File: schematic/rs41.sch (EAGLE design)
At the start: 267 parts, among them J201 SENSORBOOM, J601 expansion, J602 XDATA, Q201 BSS92, Q202 BSS92, Q203 BSS101, Q204 BSS101, Q501 BSS92, Q502 BSS101, Q503 BSS101, Q601 BSS101, U101 STM32F100C8T6B, U201 TS3A4751, U202 TS5A9411, U203 TS5A9411, U204 TS5A9411, U205 74HCU04, U206 305G, U207 74LVC3G34, U208 Z27F, U301 DIFFGEN, U302 UBX-6010MLF56, U303 SAW, U304 LNA, U401 SI4032QFN204X4, U501 TLV70030SOT23-5, U502 TPS61200, U503 TLV70030SOT23-5, U504 TLV70030SOT23-5, U601 25AA080SN, X101 24MHz, X301 OSC_GPSXTAL4

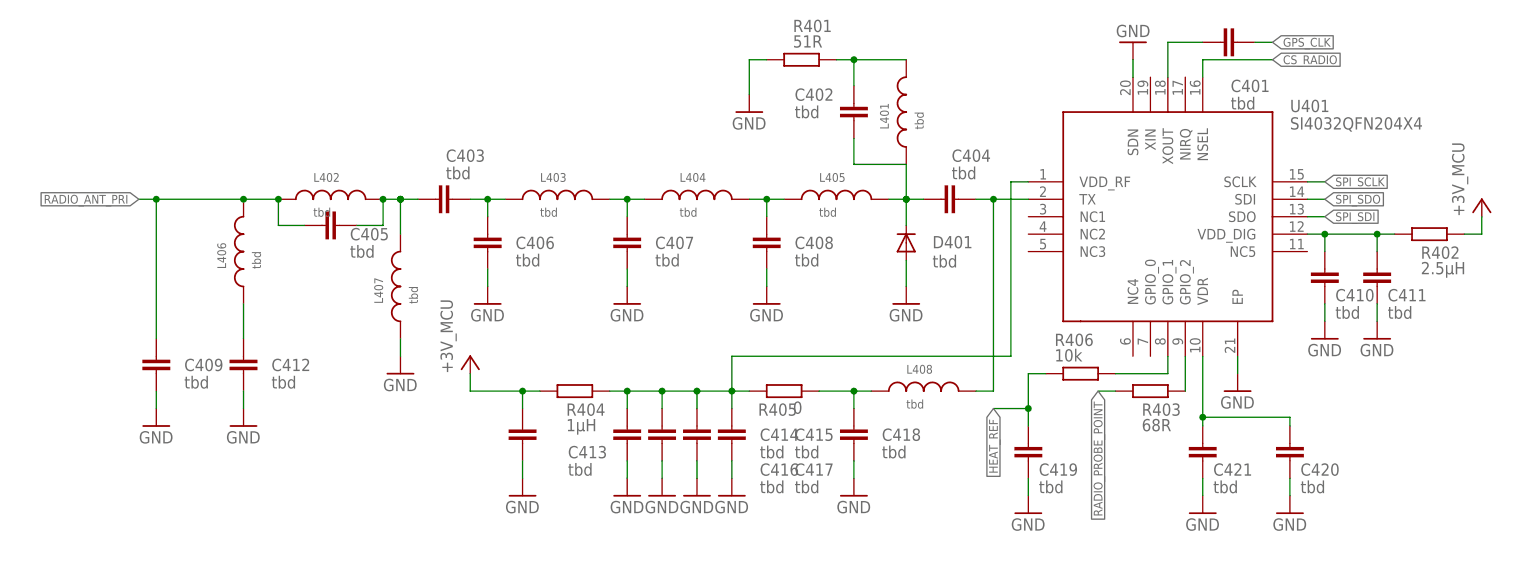
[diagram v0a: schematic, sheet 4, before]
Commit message: added missing C values
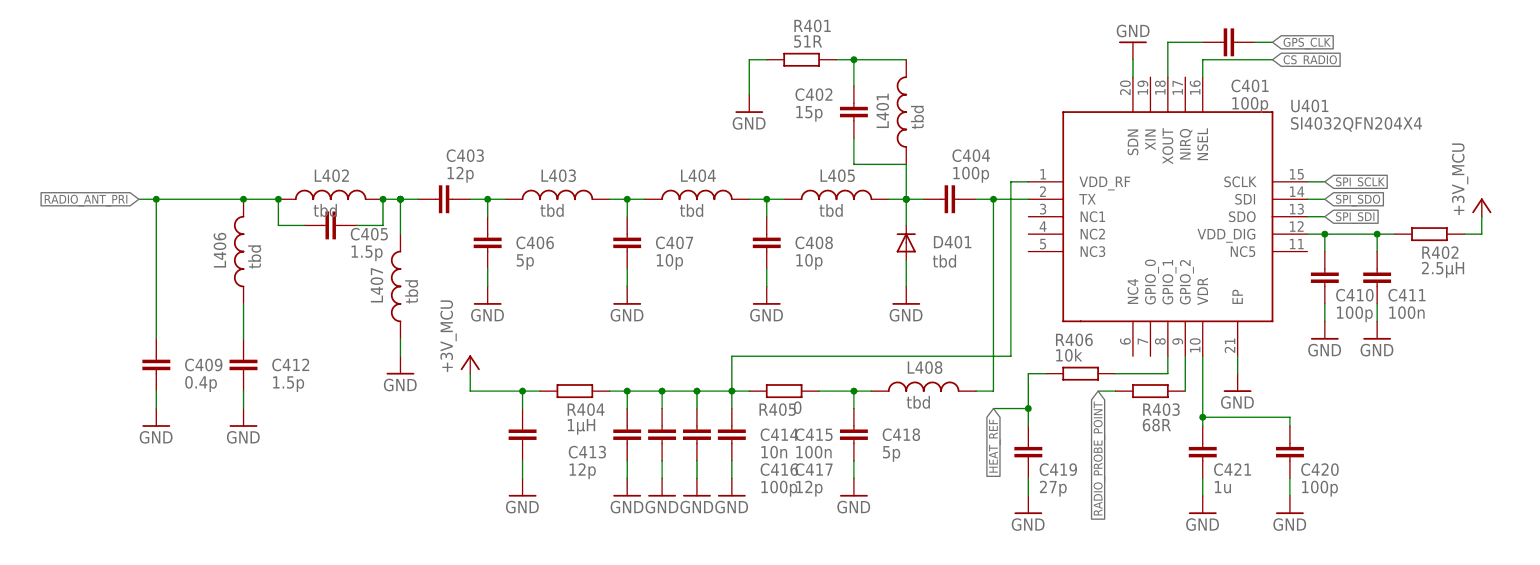
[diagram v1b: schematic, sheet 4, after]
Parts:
- C301, C303, C304, C305, C309, C311, C313, C315, C316, C319, C421: value tbd -> 1u
- C302, C307, C411, C415, C501, C510, C513, C518, C519, C520, C522, C523, C524: value tbd -> 100n
- C306, C606, C607: value tbd -> 1n
- C308, C402, C605: value tbd -> 15p
- C310: value tbd -> 6p
- C312, C314: value tbd -> 2.2u; device rcl:C-EUC0402 -> rcl:C-EUC0603
- C317, C318, C403, C413, C417, C502, C504, C509, C514, C517: value tbd -> 12p
- C401, C404, C410, C416, C420, C505: value tbd -> 100p
- C405, C412: value tbd -> 1.5p
- C406, C418: value tbd -> 5p
- C407, C408: value tbd -> 10p
- C409: value tbd -> 0.4p
- C414: value tbd -> 10n; device rcl:C-EUC0402 -> rcl:C-EUC0603
- C419: value tbd -> 27p
- C503, C515, C521: value tbd -> 10u; device rcl:C-EUC0402 -> rcl:C-EUC0603
- C506, C511, C516, C526, C602: value tbd -> 10n
- C507, C508, C512: value tbd -> 22u; device rcl:C-EUC0402 -> rcl:C-EUC0805
- C525: value tbd -> 150p
- C603: value tbd -> 200p

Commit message: small fixes, now passing ERC
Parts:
- added TP1: TPPAD1-13, testpad:TPPAD1-13
- L301, L302, L303, L304, L401, L402, L403, L404, L405, L406, L407, L408: device PowerMagnetics (rev17e):WE-MK_0402_74478410 -> rs41:LL0402
- L501: device PowerMagnetics (rev17e):WE-MAPI_3020_74438336100 -> rs41:L
- S501: value (none) -> tbd
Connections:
- removed net N$132: R122.1
- removed net SPI_SCLK: J601.15, R120.1, U401.SCLK, U601.SCK
- new net SPI_SCK: J601.15, R120.1, U601.SCK
- new net SPI_SCK_RADIO: R122.1, U401.SCLK
- net RADIO_PROBE_POINT: now also TP1.TP
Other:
- note added: "TODO: NC7SZ27 Symbol and Value"
- moved on the sheet: C201, C202, C203, C204, C205, C206, C214, C217, C405, C409, C510, J201GND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

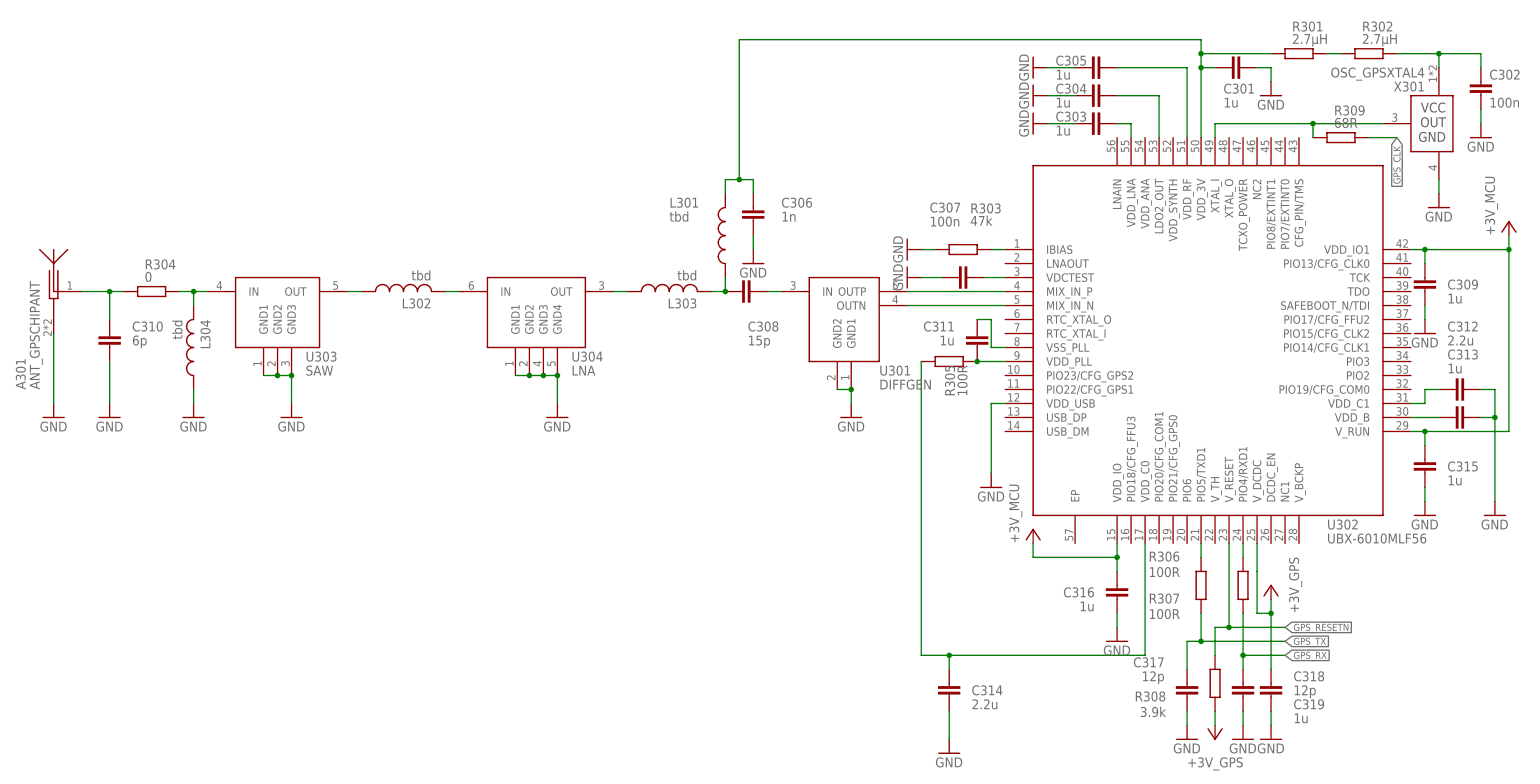
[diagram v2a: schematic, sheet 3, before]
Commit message: fixed wrong symbols and outdated readme
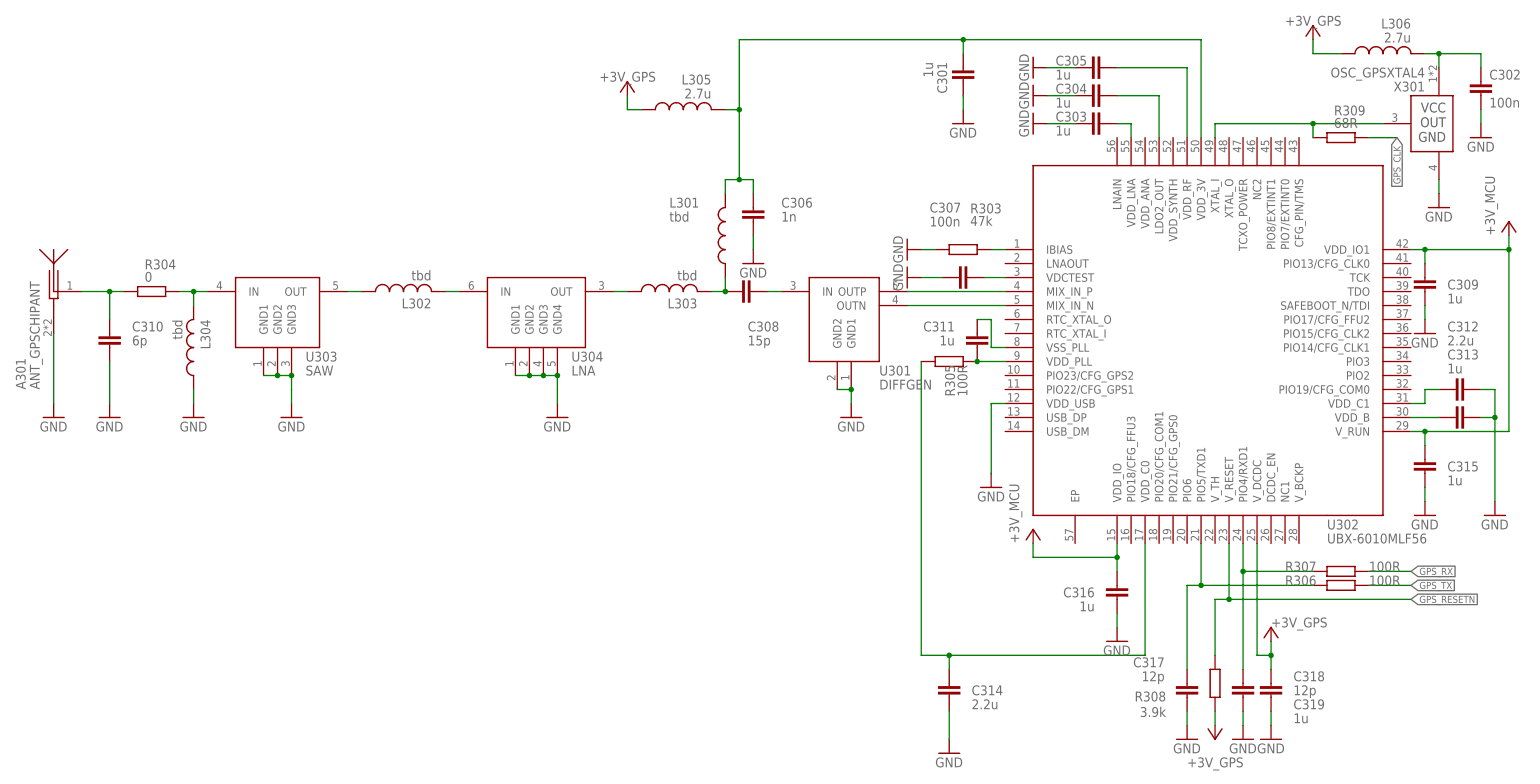
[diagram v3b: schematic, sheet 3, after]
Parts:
- removed R111: 1.9µH, rcl:R-EU_R0402
- removed R113: 2.1µH, rcl:R-EU_R0402
- removed R301, R302: 2.7µH, rcl:R-EU_R0402
- removed R402: 2.5µH, rcl:R-EU_R0402
- removed R404: 1µH, rcl:R-EU_R0402
- added L101, L102: 2u, rs41:L0402
- added L305, L306, L410: 2.7u, rs41:L0402
- added L409: 1u, rs41:L0402
- C109, C110: value 15n -> 15p
- L301, L302, L303, L304, L401, L402, L403, L404, L405, L406, L407, L408: device rs41:LL0402 -> rs41:L0402
- L501: value 2.2µH -> 2.2u; device rs41:L -> rs41:LWE3816
- R209: value 10k termistor -> 10k; device rcl:R-EU_R0402 -> rs41:THERMISTOR0402
- renumbered F502 to F501
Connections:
- net FRONTEND_UNKNOWN_1 renamed FRONTEND_UNKNOWN
- net FRONTEND_UNKNOWN_2 renamed REF_R_THERM
- removed net N$54: R301.1, R302.2
- net +3V_GPS: now also L305.1, L306.1
- net +3V_MCU: now also L409.1, L410.2; no longer R402.1, R404.2
- net GPS_RX: no longer C318.2
- net GPS_TX: no longer C317.2
- net LED_GRN: now also L101.2; no longer R111.1
- net LED_RED: now also L102.2; no longer R113.1
- net LNA_PW: now also L305.2; no longer R301.2
- net N$117: now also L102.1; no longer R113.2
- net N$119: now also L101.1; no longer R111.2
- net N$46: now also C317.2
- net N$64: now also L306.2; no longer R302.1
- net N$67: now also C318.2
- net N$73: now also L410.1; no longer R402.2
- net N$75: now also L409.2; no longer R404.1
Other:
- moved on the sheet: C301, C413, R206, R306, R307
